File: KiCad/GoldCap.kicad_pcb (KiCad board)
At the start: 2 copper layers, 38.1 x 35.6 mm, 43 parts, among them J1 Pwr In, J2 Pwr Out, J3 Main Pwr, J4 Prog, J5 Conn_01x09_Male, Q1 BC847, Q2 IRLML6401, SW1 SW_TACTILE_SPST, U1 TPS70933DBV, U2 ATtiny20-SSU

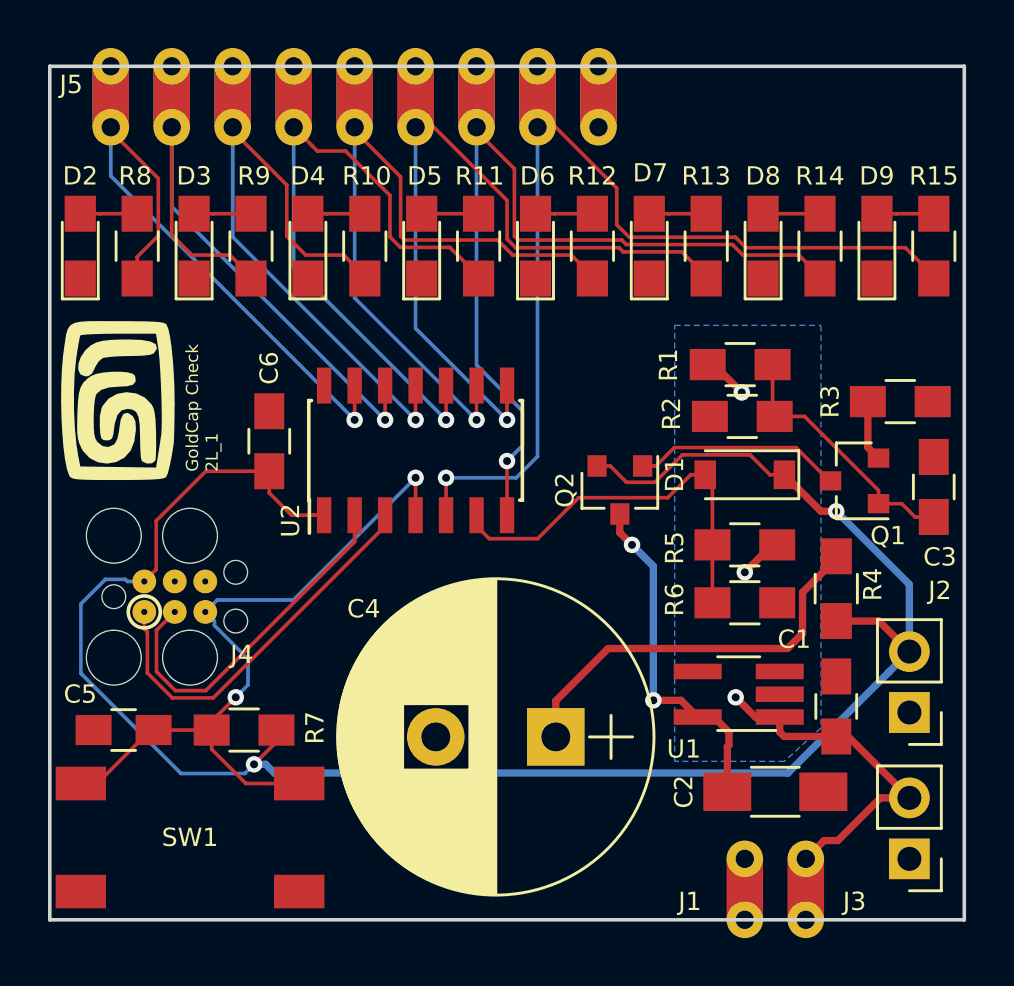
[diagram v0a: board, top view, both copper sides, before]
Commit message: Fixed some zone fills
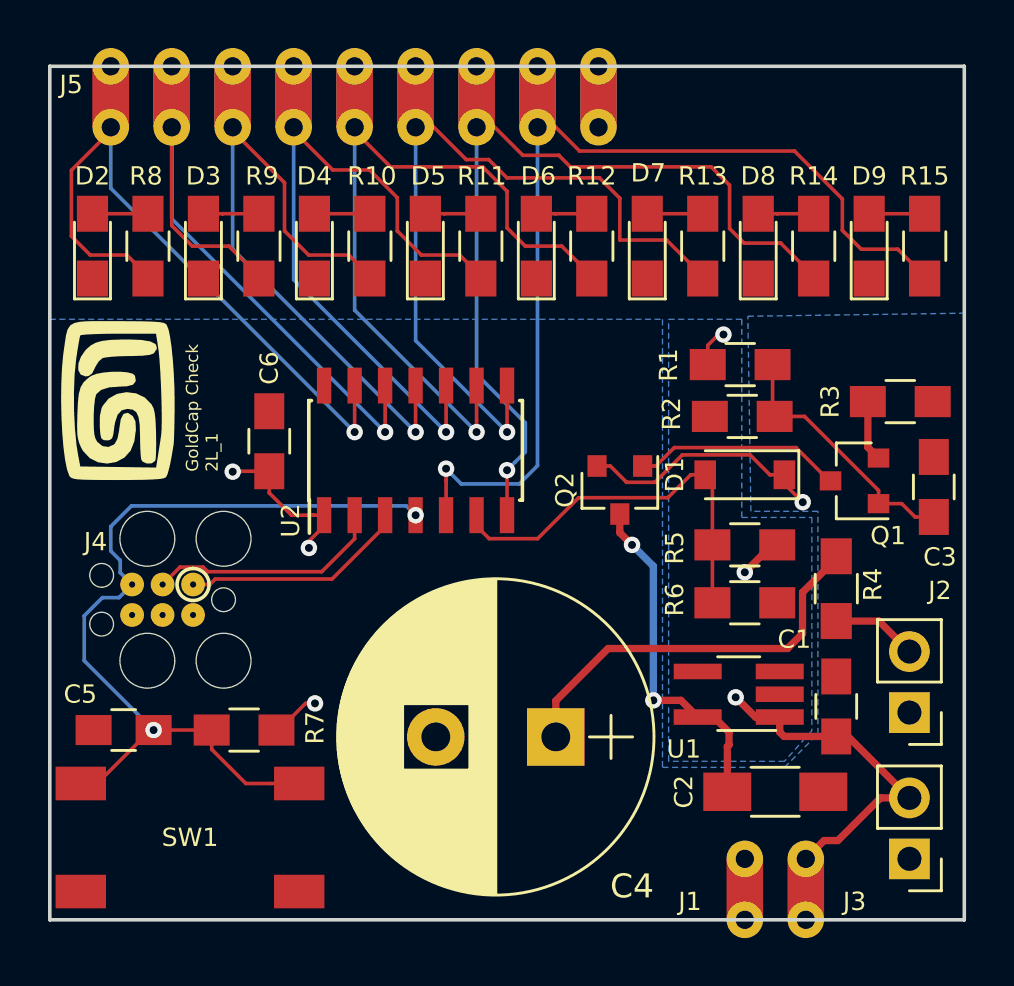
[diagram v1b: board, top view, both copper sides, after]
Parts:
- moved J4 2.33 mm to (56.8, 49.5), turned to 180 degrees
- moved D2 0.51 mm to (52.6, 35.4)
- moved R8 0.45 mm to (54.9, 35.4)
- moved D3 0.39 mm to (57.2, 35.4)
- moved R15 0.38 mm to (87.2, 35.4)
- moved R9 0.33 mm to (59.5, 35.4)
- moved D9 0.32 mm to (84.9, 35.4)
- moved D4 0.27 mm to (61.8, 35.4)
- moved R14 0.26 mm to (82.6, 35.4)
- moved R10 0.21 mm to (64.1, 35.4)
- moved D8 0.20 mm to (80.3, 35.4)
- moved D5 0.15 mm to (66.4, 35.4)
- moved R13 0.14 mm to (78.0, 35.4)
- moved R11 0.09 mm to (68.8, 35.4)
- moved D7 0.08 mm to (75.7, 35.4)
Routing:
- net /Vc: track 80.7 -> 22.7 mm, vias 2 -> 4
- net /TPIDATA: track 16.3 -> 9.46 mm
- net /~RESET: track 30.2 -> 35.8 mm
- net /TPICLK: track 15.1 -> 9.93 mm
- net /LED_PA0: track 27.9 -> 30.6 mm
- net /LED_PA1: track 28.4 -> 30.8 mm
- net /LED_PA5: track 33.0 -> 35.2 mm
- net /LED_PA4: track 32.9 -> 34.6 mm
- net /LED_PA2: track 28.8 -> 30.0 mm
- net /LED_PB2: track 43.0 -> 42.1 mm
- net /LED_PA3: track 30.3 -> 31.2 mm
- net /LED_PA6: track 39.0 -> 38.5 mm
- added copper zone on B.Cu, net /Vc

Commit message: Fixes some misplaced Vias and takes on upgrade to KiCad 5.0.2
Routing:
- net /~RESET: track 35.8 -> 42.5 mm
- net /3V3: track 14.6 -> 16.8 mm
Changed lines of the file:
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@@
-(kicad_pcb (version 20171130) (host pcbnew "(5.0.0)")
+(kicad_pcb (version 20171130) (host pcbnew "(5.0.2)-1")
   (general
     (thickness 1.6002)
     (drawings 6)
-    (tracks 247)
+    (tracks 250)
     (zones 0)
     (modules 43)
@@
     (pad_drill 0.762)
     (pad_to_mask_clearance 0)
+    (solder_mask_min_width 0.25)
     (aux_axis_origin 0 0)
     (visible_elements 7FFDFFFF)
@@
     (add_net "Net-(U1-Pad4)")
   )
+  (module GoldCap-Check:Castillation_2_2.54 (layer F.Cu)
+    (at 82.296 60.96 180)
+    (fp_text reference J1 (at 4.826 -1.778 180) (layer F.SilkS)
+      (effects (font (size 0.762 0.762) (thickness 0.127)))
+    )
+    (fp_text value "Pwr In" (at 0 -4.1 180) (layer F.Fab)
+      (effects (font (size 0.762 0.762) (thickness 0.127)))
+    )
+    (fp_line (start -1.905 -2.54) (end 4.445 -2.54) (layer F.Fab) (width 0.1))
+    (fp_line (start -1.27 1.27) (end -1.27 -2.54) (layer B.CrtYd) (width 0.01))
+    (fp_line (start -1.27 -2.54) (end 3.81 -2.54) (layer B.CrtYd) (width 0.01))
+    (fp_line (start 3.81 -2.54) (end 3.81 1.27) (layer B.CrtYd) (width 0.01))
+    (fp_line (start 3.81 1.27) (end -1.27 1.27) (layer B.CrtYd) (width 0.01))
+    (fp_line (start -1.27 1.27) (end -1.27 -2.54) (layer F.CrtYd) (width 0.01))
+    (fp_line (start 3.81 1.27) (end -1.27 1.27) (layer F.CrtYd) (width 0.01))
+    (fp_line (start 3.81 -2.54) (end 3.81 1.27) (layer F.CrtYd) (width 0.01))
+    (fp_line (start -1.27 -2.54) (end 3.81 -2.54) (layer F.CrtYd) (width 0.01))
+    (pad 2 smd rect (at 2.54 -1.27 180) (size 1.524 2.54) (layers B.Cu B.Paste B.Mask)
+      (net 1 GND))
+    (pad 1 smd rect (at 0 -1.27 180) (size 1.524 2.54) (layers B.Cu B.Paste B.Mask)
+      (net 3 /Vb))
+    (pad 2 smd rect (at 2.54 -1.27 180) (size 1.524 2.54) (layers F.Cu F.Paste F.Mask)
+      (net 1 GND))
+    (pad 1 smd rect (at 0 -1.27 180) (size 1.524 2.54) (layers F.Cu F.Paste F.Mask)
+      (net 3 /Vb))
+    (pad 2 thru_hole circle (at 2.54 -2.54 180) (size 1.524 1.524) (drill 0.762) (layers *.Cu *.Mask)
+      (net 1 GND))
+    (pad 1 thru_hole circle (at 0 -2.54 180) (size 1.524 1.524) (drill 0.762) (layers *.Cu *.Mask)
+      (net 3 /Vb))
+    (pad 2 thru_hole circle (at 2.54 0 180) (size 1.524 1.524) (drill 0.762) (layers *.Cu *.Mask)
+      (net 1 GND))
+    (pad 1 thru_hole circle (at 0 0 180) (size 1.524 1.524) (drill 0.762) (layers *.Cu *.Mask)
+      (net 3 /Vb))
+  )
   (module GoldCap-Check:PRG_TC2030-IDC-FP_TH (layer F.Cu)
     (at 56.769 49.53 180)
@@
       (rotate (xyz 0 0 0))
     )
-  )
-  (module GoldCap-Check:Castillation_2_2.54 (layer F.Cu)
-    (at 82.296 60.96 180)
-    (fp_text reference J1 (at 4.826 -1.778 180) (layer F.SilkS)
-      (effects (font (size 0.762 0.762) (thickness 0.127)))
-    )
-    (fp_text value "Pwr In" (at 0 -4.1 180) (layer F.Fab)
-      (effects (font (size 0.762 0.762) (thickness 0.127)))
-    )
-    (fp_line (start -1.27 -2.54) (end 3.81 -2.54) (layer F.CrtYd) (width 0.01))
-    (fp_line (start 3.81 -2.54) (end 3.81 1.27) (layer F.CrtYd) (width 0.01))
-    (fp_line (start 3.81 1.27) (end -1.27 1.27) (layer F.CrtYd) (width 0.01))
-    (fp_line (start -1.27 1.27) (end -1.27 -2.54) (layer F.CrtYd) (width 0.01))
-    (fp_line (start 3.81 1.27) (end -1.27 1.27) (layer B.CrtYd) (width 0.01))
-    (fp_line (start 3.81 -2.54) (end 3.81 1.27) (layer B.CrtYd) (width 0.01))
-    (fp_line (start -1.27 -2.54) (end 3.81 -2.54) (layer B.CrtYd) (width 0.01))
-    (fp_line (start -1.27 1.27) (end -1.27 -2.54) (layer B.CrtYd) (width 0.01))
-    (fp_line (start -1.905 -2.54) (end 4.445 -2.54) (layer F.Fab) (width 0.1))
-    (pad 1 thru_hole circle (at 0 0 180) (size 1.524 1.524) (drill 0.762) (layers *.Cu *.Mask)
-      (net 3 /Vb))
-    (pad 2 thru_hole circle (at 2.54 0 180) (size 1.524 1.524) (drill 0.762) (layers *.Cu *.Mask)
-      (net 1 GND))
-    (pad 1 thru_hole circle (at 0 -2.54 180) (size 1.524 1.524) (drill 0.762) (layers *.Cu *.Mask)
-      (net 3 /Vb))
-    (pad 2 thru_hole circle (at 2.54 -2.54 180) (size 1.524 1.524) (drill 0.762) (layers *.Cu *.Mask)
-      (net 1 GND))
-    (pad 1 smd rect (at 0 -1.27 180) (size 1.524 2.54) (layers *.Paste *.Mask F.Cu)
-      (net 3 /Vb))
-    (pad 2 smd rect (at 2.54 -1.27 180) (size 1.524 2.54) (layers *.Paste *.Mask F.Cu)
-      (net 1 GND))
   )
   (module Pin_Headers:Pin_Header_Straight_1x02_Pitch2.54mm (layer F.Cu)
@@
   (segment (start 79.026 56.286) (end 79.0968 56.2152) (width 0.3048) (layer F.Cu) (net 4))
   (segment (start 79.026 58.166) (end 79.026 56.286) (width 0.3048) (layer F.Cu) (net 4))
-  (via (at 75.057 47.879) (size 0.6858) (drill 0.3302) (layers F.Cu B.Cu) (net 4))
-  (segment (start 74.549 46.593) (end 74.549 47.371) (width 0.3048) (layer F.Cu) (net 4))
-  (segment (start 74.549 47.371) (end 75.057 47.879) (width 0.3048) (layer F.Cu) (net 4))
-  (via (at 75.946 54.356) (size 0.6858) (drill 0.3302) (layers F.Cu B.Cu) (net 4))
-  (segment (start 75.057 47.879) (end 75.946 48.768) (width 0.3048) (layer B.Cu) (net 4))
-  (segment (start 75.946 48.768) (end 75.946 54.356) (width 0.3048) (layer B.Cu) (net 4))
-  (segment (start 77.096 54.356) (end 77.792 55.052) (width 0.3048) (layer F.Cu) (net 4))
-  (segment (start 75.946 54.356) (end 77.096 54.356) (width 0.3048) (layer F.Cu) (net 4))
+  (via (at 77.216 56.515) (size 0.6858) (drill 0.3302) (layers F.Cu B.Cu) (net 4))
+  (segment (start 77.792 55.052) (end 77.792 55.939) (width 0.1524) (layer F.Cu) (net 4))
+  (segment (start 77.792 55.939) (end 77.216 56.515) (width 0.1524) (layer F.Cu) (net 4))
+  (via (at 74.549 48.006) (size 0.6858) (drill 0.3302) (layers F.Cu B.Cu) (net 4))
+  (segment (start 74.549 46.593) (end 74.549 48.006) (width 0.1524) (layer F.Cu) (net 4))
+  (segment (start 74.549 53.848) (end 77.216 56.515) (width 0.1524) (layer B.Cu) (net 4))
+  (segment (start 74.549 48.006) (end 74.549 53.848) (width 0.1524) (layer B.Cu) (net 4))
   (segment (start 71.882 54.3752) (end 71.882 55.88) (width 0.3048) (layer F.Cu) (net 5))
   (segment (start 83.566 48.354) (end 83.566 48.454) (width 0.3048) (layer F.Cu) (net 5))
@@
   (segment (start 81.534 52.197) (end 74.0602 52.197) (width 0.3048) (layer F.Cu) (net 5))
   (segment (start 74.0602 52.197) (end 71.882 54.3752) (width 0.3048) (layer F.Cu) (net 5))
-  (segment (start 52.77271 57.821) (end 54.999455 55.594255) (width 0.1524) (layer F.Cu) (net 6))
   (segment (start 52.092 57.821) (end 52.77271 57.821) (width 0.1524) (layer F.Cu) (net 6))
   (segment (start 59.9896 57.821) (end 61.192 57.821) (width 0.1524) (layer F.Cu) (net 6))
@@
   (segment (start 55.124459 55.594251) (end 55.124455 55.594255) (width 0.1524) (layer F.Cu) (net 6))
   (segment (start 57.544455 55.594251) (end 55.124459 55.594251) (width 0.1524) (layer F.Cu) (net 6))
-  (via (at 55.124455 55.594255) (size 0.6858) (drill 0.3302) (layers F.Cu B.Cu) (net 6))
-  (segment (start 52.235099 52.704899) (end 55.124455 55.594255) (width 0.1524) (layer B.Cu) (net 6))
-  (segment (start 52.235099 50.833527) (end 52.235099 52.704899) (width 0.1524) (layer B.Cu) (net 6))
+  (segment (start 53.733701 48.524671) (end 53.34 48.13097) (width 0.1524) (layer B.Cu) (net 6))
+  (segment (start 54.229 49.53) (end 53.733701 49.034701) (width 0.1524) (layer B.Cu) (net 6))
+  (segment (start 53.733701 49.034701) (end 53.733701 48.524671) (width 0.1524) (layer B.Cu) (net 6))
+  (via (at 66.04 44.704) (size 0.6858) (drill 0.3302) (layers F.Cu B.Cu) (net 6))
+  (segment (start 64.490601 46.253399) (end 66.04 44.704) (width 0.1524) (layer B.Cu) (net 6))
+  (segment (start 54.205631 46.253399) (end 64.490601 46.253399) (width 0.1524) (layer B.Cu) (net 6))
+  (segment (start 53.34 48.13097) (end 53.34 47.11903) (width 0.1524) (layer B.Cu) (net 6))
+  (segment (start 53.34 47.11903) (end 54.205631 46.253399) (width 0.1524) (layer B.Cu) (net 6))
+  (segment (start 66.04 44.704) (end 66.04 46.642) (width 0.1524) (layer F.Cu) (net 6))
+  (via (at 55.118 57.785) (size 0.6858) (drill 0.3302) (layers F.Cu B.Cu) (net 6))
+  (segment (start 52.235099 54.902099) (end 55.118 57.785) (width 0.1524) (layer B.Cu) (net 6))
+  (segment (start 52.235099 50.833527) (end 52.235099 54.902099) (width 0.1524) (layer B.Cu) (net 6))
   (segment (start 52.992527 50.076099) (end 52.235099 50.833527) (width 0.1524) (layer B.Cu) (net 6))
   (segment (start 54.229 49.53) (end 53.682901 50.076099) (width 0.1524) (layer B.Cu) (net 6))
   (segment (start 53.682901 50.076099) (end 52.992527 50.076099) (width 0.1524) (layer B.Cu) (net 6))
-  (segment (start 53.733701 48.524671) (end 53.34 48.13097) (width 0.1524) (layer B.Cu) (net 6))
-  (segment (start 54.229 49.53) (end 53.733701 49.034701) (width 0.1524) (layer B.Cu) (net 6))
-  (segment (start 53.733701 49.034701) (end 53.733701 48.524671) (width 0.1524) (layer B.Cu) (net 6))
-  (via (at 66.04 46.642) (size 0.6858) (drill 0.3302) (layers F.Cu B.Cu) (net 6))
-  (segment (start 65.651399 46.253399) (end 66.04 46.642) (width 0.1524) (layer B.Cu) (net 6))
-  (segment (start 54.205631 46.253399) (end 65.651399 46.253399) (width 0.1524) (layer B.Cu) (net 6))
-  (segment (start 53.34 47.11903) (end 54.205631 46.253399) (width 0.1524) (layer B.Cu) (net 6))
-  (segment (start 53.34 48.13097) (end 53.34 47.11903) (width 0.1524) (layer B.Cu) (net 6))
+  (segment (start 55.118 55.60071) (end 55.124455 55.594255) (width 0.1524) (layer F.Cu) (net 6))
+  (segment (start 55.118 57.785) (end 55.118 55.60071) (width 0.1524) (layer F.Cu) (net 6))
+  (segment (start 52.128 57.785) (end 52.092 57.821) (width 0.1524) (layer F.Cu) (net 6))
+  (segment (start 55.118 57.785) (end 52.128 57.785) (width 0.1524) (layer F.Cu) (net 6))
   (segment (start 78.406 50.292) (end 78.406 47.879) (width 0.1524) (layer F.Cu) (net 7))
   (segment (start 78.406 45.258) (end 78.106 44.958) (width 0.1524) (layer F.Cu) (net 7))
